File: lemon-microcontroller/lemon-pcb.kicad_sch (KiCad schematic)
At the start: 52 parts, among them J1 USB_C_Receptacle_USB2.0, J2 USB_C_Receptacle_USB2.0, J3 Conn_01x11, J5 Conn_01x11, Q1 Q_NMOS, Q2 Q_PMOS_SGD, SW1 SW_Push, SW2 SW_Push, U1 W25Q128JVS, U2 USBLC6-2SC6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

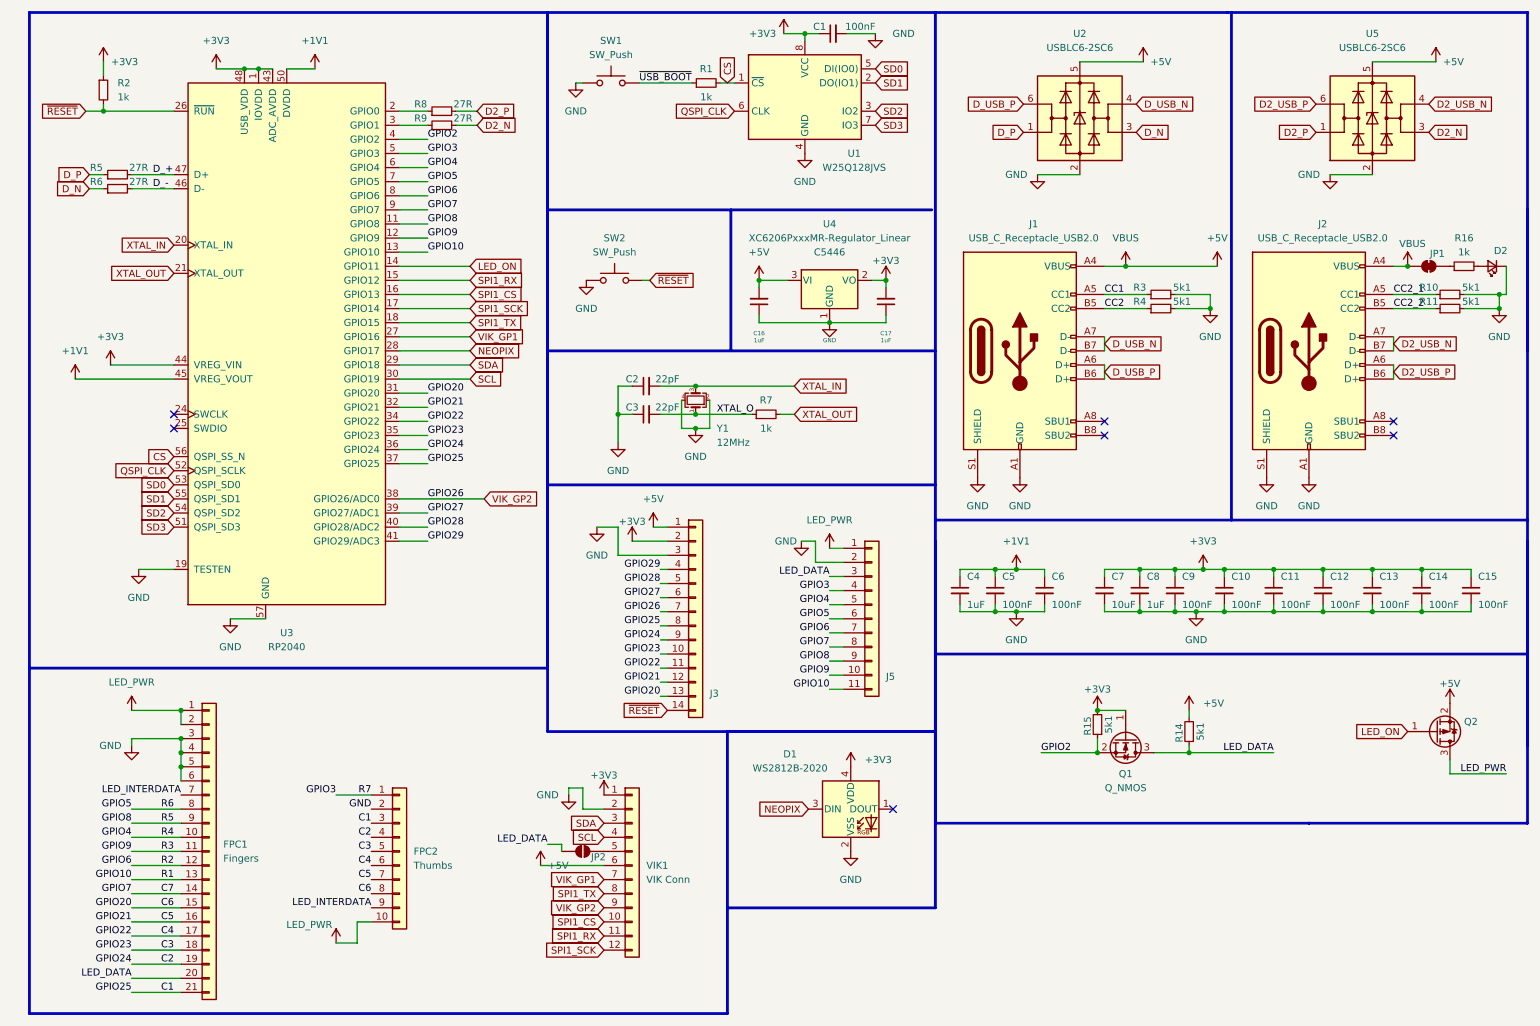
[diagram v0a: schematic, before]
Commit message: Update Wired Lemon V03 information
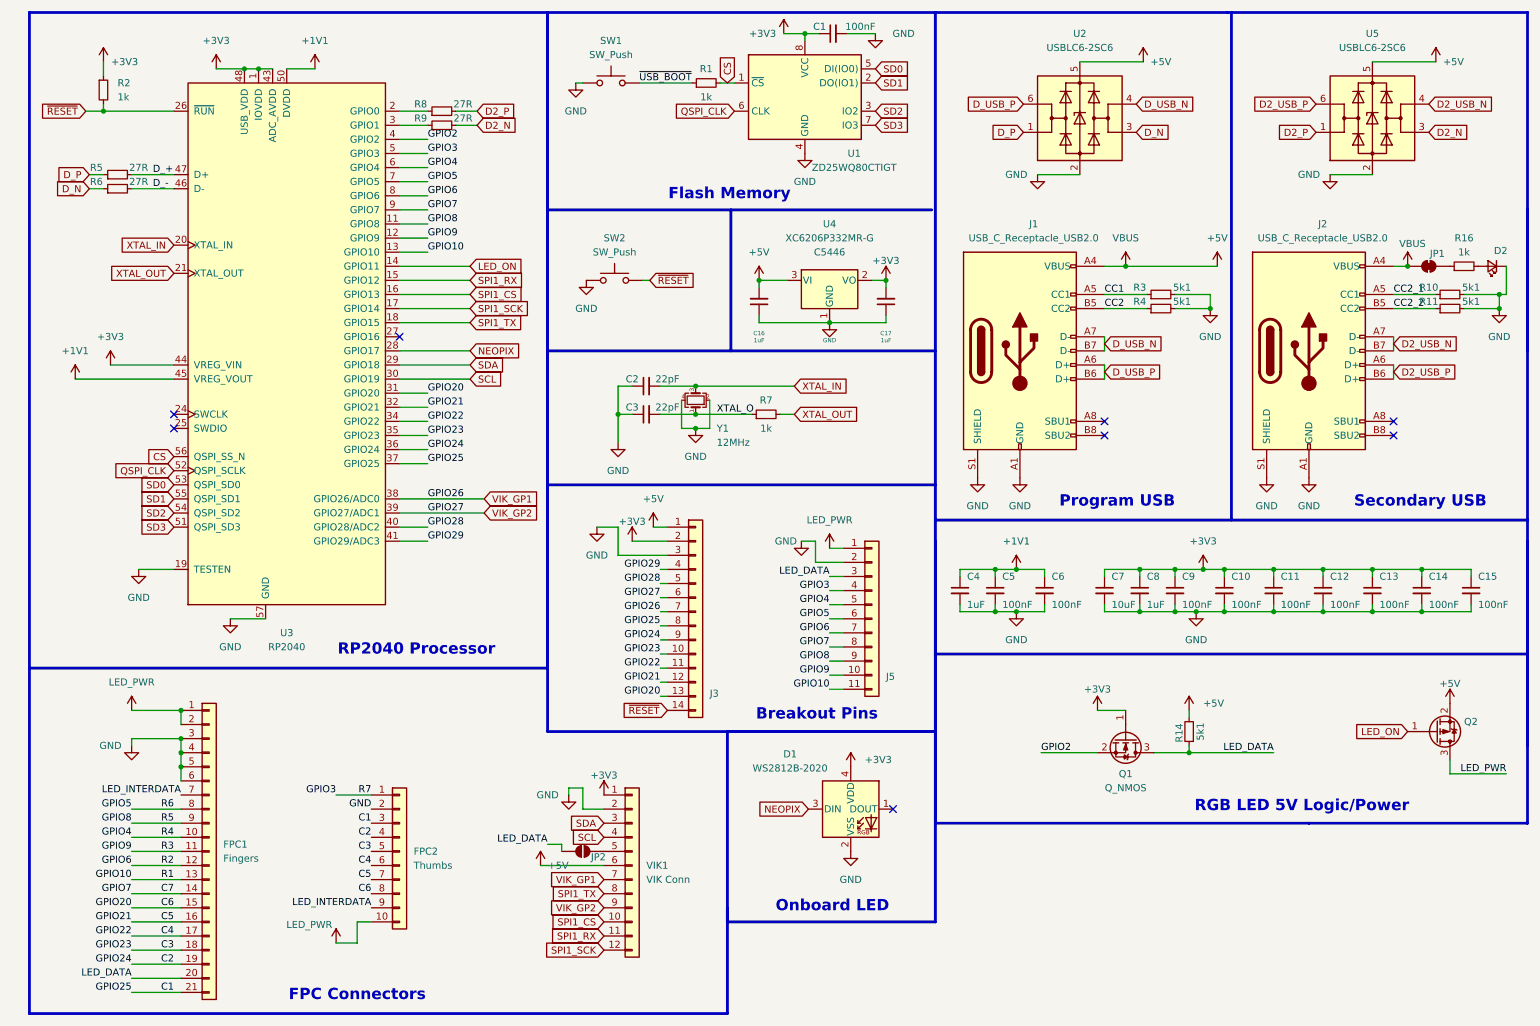
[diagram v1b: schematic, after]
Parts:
- removed R15: 5k1, Resistor_SMD:R_0402_1005Metric, symbol Device:R_Small
- U1: value W25Q128JVS -> ZD25WQ80CTIGT
- U4: value XC6206PxxxMR-Regulator_Linear -> XC6206P332MR-G
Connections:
- net GPIO27 is gone; now on net VIK_GP2: J3.6 (Pin_6), U3.39 (GPIO27/ADC1)
- net VIK_GP1: now also J3.7 (Pin_7), U3.38 (GPIO26/ADC0); no longer U3.27 (GPIO16)
- net VIK_GP2: no longer J3.7 (Pin_7), U3.38 (GPIO26/ADC0)
- no-connect marks 7 -> 8
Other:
- note added: "Breakout Pins"
- note added: "FPC Connectors"
- note added: "Flash Memory"
- note added: "Onboard LED"
- note added: "Program USB"
- note added: "RGB LED 5V Logic/Power"
- note added: "RP2040 Processor"
- note added: "Secondary USB"
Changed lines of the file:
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@@
 (kicad_sch
-	(version 20231120)
+	(version 20250114)
 	(generator "eeschema")
-	(generator_version "8.0")
+	(generator_version "9.0")
 	(paper "A4")
 	(title_block
@@
 		(company "Cosmos Keyboards")
 	)
+	(rectangle
+		(start 139.065 143.51)
+		(end 176.53 177.8)
+		(stroke
+			(width 0.5)
+			(type default)
+		)
+		(fill
+			(type none)
+		)
+	)
+	(rectangle
+		(start 13.335 13.97)
+		(end 106.68 132.08)
+		(stroke
+			(width 0.5)
+			(type default)
+		)
+		(fill
+			(type none)
+		)
+	)
+	(text "FPC Connectors"
+		(exclude_from_sim no)
+		(at 72.39 191.008 0)
+		(effects
+			(font
+				(size 2.032 2.032)
+				(thickness 0.508)
+				(bold yes)
+			)
+		)
+	)
+	(text "Program USB"
+		(exclude_from_sim no)
+		(at 209.296 102.108 0)
+		(effects
+			(font
+				(size 2.032 2.032)
+				(thickness 0.508)
+				(bold yes)
+			)
+		)
+	)
+	(text "RP2040 Processor"
+		(exclude_from_sim no)
+		(at 83.058 128.778 0)
+		(effects
+			(font
+				(size 2.032 2.032)
+				(thickness 0.508)
+				(bold yes)
+			)
+		)
+	)
+	(text "Secondary USB"
+		(exclude_from_sim no)
+		(at 263.906 102.108 0)
+		(effects
+			(font
+				(size 2.032 2.032)
+				(thickness 0.508)
+				(bold yes)
+			)
+		)
+	)
+	(text "Breakout Pins"
+		(exclude_from_sim no)
+		(at 155.194 140.462 0)
+		(effects
+			(font
+				(size 2.032 2.032)
+				(thickness 0.508)
+				(bold yes)
+			)
+		)
+	)
+	(text "Onboard LED"
+		(exclude_from_sim no)
+		(at 157.988 175.006 0)
+		(effects
+			(font
+				(size 2.032 2.032)
+				(thickness 0.508)
+				(bold yes)
+			)
+		)
+	)
+	(text "Flash Memory"
+		(exclude_from_sim no)
+		(at 139.446 46.736 0)
+		(effects
+			(font
+				(size 2.032 2.032)
+				(thickness 0.508)
+				(bold yes)
+			)
+		)
+	)
+	(text "RGB LED 5V Logic/Power"
+		(exclude_from_sim no)
+		(at 242.57 156.972 0)
+		(effects
+			(font
+				(size 2.032 2.032)
+				(thickness 0.508)
+				(bold yes)
+			)
+		)
+	)
 	(junction
 		(at 133.35 88.9)
@@
 	)
 	(junction
-		(at 205.74 139.7)
-		(diameter 0)
-		(color 0 0 0 0)
-	)
-	(junction
 		(at 278.13 64.77)
 		(diameter 0)
@@
 	)
 	(junction
-		(at 205.74 147.32)
-		(diameter 0)
-		(color 0 0 0 0)
-	)
-	(junction
 		(at 191.135 121.92)
 		(diameter 0)
@@
 	)
 	(no_connect
+		(at 80.01 72.39)
+	)
+	(no_connect
 		(at 39.37 86.36)
 	)
@@
 	(wire
 		(pts
-			(xy 205.74 144.78) (xy 205.74 147.32)
-		)
-		(stroke
-			(width 0)
-			(type default)
-		)
-	)
-	(wire
-		(pts
 			(xy 271.78 64.77) (xy 278.13 64.77)
 		)
@@
 	(wire
 		(pts
+			(xy 80.01 104.14) (xy 95.25 104.14)
+		)
+		(stroke
+			(width 0)
+			(type default)
+		)
+	)
+	(wire
+		(pts
 			(xy 119.38 111.76) (xy 128.27 111.76)
 		)
@@
 		)
 	)
-	(wire
-		(pts
-			(xy 80.01 72.39) (xy 92.71 72.39)
-		)
-		(stroke
-			(width 0)
-			(type default)
-		)
-	)
 	(polyline
 		(pts
@@
 	(wire
 		(pts
-			(xy 85.09 104.14) (xy 80.01 104.14)
-		)
-		(stroke
-			(width 0)
-			(type default)
-		)
-	)
-	(wire
-		(pts
 			(xy 80.01 74.93) (xy 92.71 74.93)
 		)
@@
 		)
 	)
-	(rectangle
-		(start 139.065 143.51)
-		(end 176.53 175.26)
-		(stroke
-			(width 0.5)
-			(type default)
-		)
-		(fill
-			(type none)
-		)
-	)
-	(rectangle
-		(start 13.335 13.97)
-		(end 106.68 132.08)
-		(stroke
-			(width 0.5)
-			(type default)
-		)
-		(fill
-			(type none)
-		)
-	)
 	(label "GPIO28"
 		(at 85.09 106.68 0)
@@
 	(global_label "VIK_GP2"
 		(shape input)
-		(at 95.25 101.6 0)
+		(at 95.25 104.14 0)
 		(fields_autoplaced yes)
 		(effects
@@
 		)
 		(property "Intersheetrefs" "${INTERSHEET_REFS}"
-			(at 105.9157 101.6 0)
+			(at 105.9157 104.14 0)
 			(effects
 				(font
@@
 	(global_label "VIK_GP1"
 		(shape input)
-		(at 92.71 72.39 0)
+		(at 95.25 101.6 0)
 		(fields_autoplaced yes)
 		(effects
@@
 		)
 		(property "Intersheetrefs" "${INTERSHEET_REFS}"
-			(at 103.3757 72.39 0)
+			(at 105.9157 101.6 0)
 			(effects
 				(font
@@
 	)
 	(symbol
-		(lib_id "Device:R_Small")
-		(at 205.74 142.24 180)
-		(unit 1)
-		(exclude_from_sim no)
-		(in_bom yes)
-		(on_board yes)
-		(dnp no)
-		(property "Reference" "R15"
-			(at 203.962 142.494 90)
-			(effects
-				(font
-					(size 1.27 1.27)
-				)
-			)
-		)
-		(property "Value" "5k1"
-			(at 207.772 142.24 90)
-			(effects
-				(font
-					(size 1.27 1.27)
-				)
-			)
-		)
-		(property "Footprint" "Resistor_SMD:R_0402_1005Metric"
-			(at 205.74 142.24 0)
-			(effects
-				(font
-					(size 1.27 1.27)
-				)
-				(hide yes)
-			)
-		)
-		(property "Datasheet" "~"
-			(at 205.74 142.24 0)
-			(effects
-				(font
-					(size 1.27 1.27)
-				)
-				(hide yes)
-			)
-		)
-		(property "Description" ""
-			(at 205.74 142.24 0)
-			(effects
-				(font
-					(size 1.27 1.27)
-				)
-				(hide yes)
-			)
-		)
-		(property "LCSC" "C25905"
-			(at 205.74 142.24 0)
-			(effects
-				(font
-					(size 1.27 1.27)
-				)
-				(hide yes)
-			)
-		)
-		(pin "1"
-		)
-		(pin "2"
-		)
-		(instances
-			(project "lemon-pcb"
-				(path "/ba62e47e-9e07-4e97-ab08-24b670d50f97"
-					(reference "R15")
-					(unit 1)
-				)
-			)
-		)
-	)
-	(symbol
 		(lib_id "power:+3V3")
 		(at 224.79 114.3 0)
@@
 			)
 		)
-		(property "Value" "W25Q128JVS"
+		(property "Value" "ZD25WQ80CTIGT"
 			(at 161.925 41.91 0)
 			(effects
@@
 			)
 		)
-		(property "Value" "XC6206PxxxMR-Regulator_Linear"
+		(property "Value" "XC6206P332MR-G"
 			(at 157.48 54.61 0)
 			(effects
@@
 		)
 	)
+	(embedded_fonts no)
 )

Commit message: Lemon wired V0.4, Lemon wireless V0.3
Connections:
- net C7: now also J5.11 (Pin_11), U3.13 (GPIO10); no longer J5.8 (Pin_8), U3.9 (GPIO7)
- removed net GPIO10: FPC1.13 (Pin_13), J5.11 (Pin_11), U3.13 (GPIO10)
- net GPIO2 renamed RGB
- net GPIO3 renamed R1
- net R1: now also FPC1.13 (Pin_13); no longer FPC2.1 (Pin_1)
- net GPIO4 renamed R2
- net R2: now also FPC1.12 (Pin_12); no longer FPC1.10 (Pin_10)
- net GPIO5 renamed R3
- net R3: now also FPC1.11 (Pin_11); no longer FPC1.8 (Pin_8)
- net GPIO6 renamed R4
- net R4: now also FPC1.10 (Pin_10); no longer FPC1.12 (Pin_12)
- net GPIO8 renamed R6
- net R6: now also FPC1.8 (Pin_8); no longer FPC1.9 (Pin_9)
- net GPIO9 renamed R7
- net R7: now also FPC2.1 (Pin_1); no longer FPC1.11 (Pin_11)
- new net R5: FPC1.9 (Pin_9), J5.8 (Pin_8), U3.9 (GPIO7)
